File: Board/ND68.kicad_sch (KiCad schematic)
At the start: 8 parts

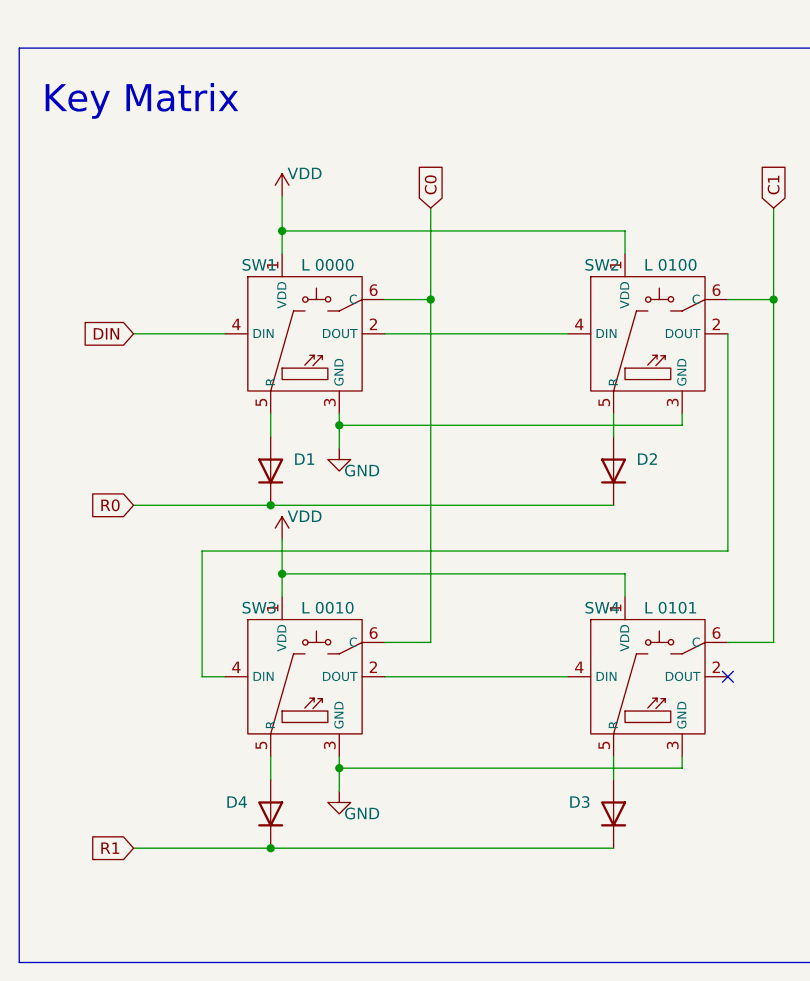
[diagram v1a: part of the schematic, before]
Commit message: Done routing all parts.
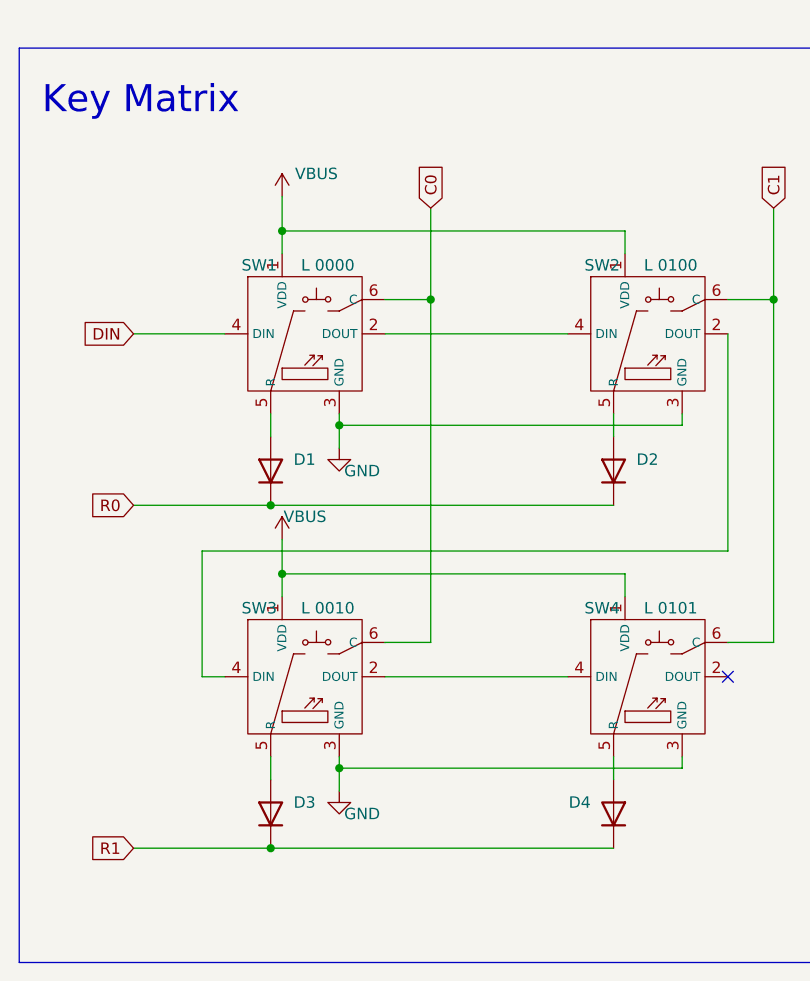
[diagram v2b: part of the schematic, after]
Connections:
- net at SW4.5 (R): now also D4.2 (A); no longer D3.2 (A)
- net at SW3.5 (R): now also D3.2 (A); no longer D4.2 (A)
- net VDD renamed VBUS
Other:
- moved on the sheet: D3, D4
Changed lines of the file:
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@@
   (junction (at 118.11 96.52) (diameter 0) (color 0 0 0 0)
   )
+  (junction (at 124.46 118.11) (diameter 0) (color 0 0 0 0)
+  )
+  (junction (at 116.84 88.9) (diameter 0) (color 0 0 0 0)
+  )
+  (junction (at 118.11 58.42) (diameter 0) (color 0 0 0 0)
+  )
+  (junction (at 124.46 80.01) (diameter 0) (color 0 0 0 0)
+  )
+  (junction (at 172.72 66.04) (diameter 0) (color 0 0 0 0)
+  )
   (junction (at 116.84 127) (diameter 0) (color 0 0 0 0)
-  )
-  (junction (at 124.46 118.11) (diameter 0) (color 0 0 0 0)
-  )
-  (junction (at 116.84 88.9) (diameter 0) (color 0 0 0 0)
-  )
-  (junction (at 118.11 58.42) (diameter 0) (color 0 0 0 0)
-  )
-  (junction (at 124.46 80.01) (diameter 0) (color 0 0 0 0)
-  )
-  (junction (at 172.72 66.04) (diameter 0) (color 0 0 0 0)
   )
   (junction (at 134.62 66.04) (diameter 0) (color 0 0 0 0)
@@
     (stroke (width 0) (type default))
   )
+  (wire (pts (xy 109.22 107.95) (xy 111.76 107.95))
+    (stroke (width 0) (type default))
+  )
+  (wire (pts (xy 101.6 69.85) (xy 111.76 69.85))
+    (stroke (width 0) (type default))
+  )
+  (wire (pts (xy 162.56 116.84) (xy 162.56 118.11))
+    (stroke (width 0) (type default))
+  )
+  (wire (pts (xy 162.56 78.74) (xy 162.56 80.01))
+    (stroke (width 0) (type default))
+  )
   (wire (pts (xy 116.84 127) (xy 154.94 127))
-    (stroke (width 0) (type default))
-  )
-  (wire (pts (xy 109.22 107.95) (xy 111.76 107.95))
-    (stroke (width 0) (type default))
-  )
-  (wire (pts (xy 101.6 69.85) (xy 111.76 69.85))
-    (stroke (width 0) (type default))
-  )
-  (wire (pts (xy 162.56 116.84) (xy 162.56 118.11))
-    (stroke (width 0) (type default))
-  )
-  (wire (pts (xy 162.56 78.74) (xy 162.56 80.01))
     (stroke (width 0) (type default))
   )
@@
     )
   )
-  (symbol (lib_id "power:VDD") (at 118.11 54.61 0) (unit 1)
+  (symbol (lib_id "power:VBUS") (at 118.11 92.71 0) (unit 1)
     (in_bom yes) (on_board yes) (dnp no)
-    (property "Reference" "#PWR028" (at 118.11 58.42 0)
-      (effects (font (size 1.27 1.27)) hide)
-    )
-    (property "Value" "VDD" (at 120.65 52.07 0)
-      (effects (font (size 1.27 1.27)))
-    )
-    (property "Footprint" "" (at 118.11 54.61 0)
-      (effects (font (size 1.27 1.27)) hide)
-    )
-    (property "Datasheet" "" (at 118.11 54.61 0)
+    (property "Reference" "#PWR028" (at 118.11 96.52 0)
+      (effects (font (size 1.27 1.27)) hide)
+    )
+    (property "Value" "VBUS" (at 120.65 90.17 0)
+      (effects (font (size 1.27 1.27)))
+    )
+    (property "Footprint" "" (at 118.11 92.71 0)
+      (effects (font (size 1.27 1.27)) hide)
+    )
+    (property "Datasheet" "" (at 118.11 92.71 0)
       (effects (font (size 1.27 1.27)) hide)
     )
@@
     )
   )
-  (symbol (lib_id "power:VDD") (at 118.11 92.71 0) (unit 1)
-    (in_bom yes) (on_board yes) (dnp no)
-    (property "Reference" "#PWR029" (at 118.11 96.52 0)
-      (effects (font (size 1.27 1.27)) hide)
-    )
-    (property "Value" "VDD" (at 120.65 90.17 0)
-      (effects (font (size 1.27 1.27)))
-    )
-    (property "Footprint" "" (at 118.11 92.71 0)
-      (effects (font (size 1.27 1.27)) hide)
-    )
-    (property "Datasheet" "" (at 118.11 92.71 0)
-      (effects (font (size 1.27 1.27)) hide)
-    )
-    (pin "1")
-    (instances
-      (project "ND68"
-        (path "/f6515d16-f8c0-46c5-adb6-b60d73ae282b"
-          (reference "#PWR029") (unit 1)
-        )
-      )
-    )
-  )
   (symbol (lib_id "Device:D") (at 154.94 85.09 90) (unit 1)
     (in_bom yes) (on_board yes) (dnp no) (fields_autoplaced)
@@
     )
   )
-  (symbol (lib_id "Device:D") (at 154.94 123.19 270) (mirror x) (unit 1)
-    (in_bom yes) (on_board yes) (dnp no) (fields_autoplaced)
-    (property "Reference" "D3" (at 152.4 121.92 90)
+  (symbol (lib_id "Device:D") (at 116.84 123.19 90) (unit 1)
+    (in_bom yes) (on_board yes) (dnp no)
+    (property "Reference" "D3" (at 119.38 121.92 90)
       (effects (font (size 1.27 1.27)) (justify right))
     )
-    (property "Value" "D" (at 152.4 124.46 90)
-      (effects (font (size 1.27 1.27)) (justify right) hide)
-    )
-    (property "Footprint" "Diode_SMD:D_SOD-123F" (at 154.94 123.19 0)
-      (effects (font (size 1.27 1.27)) hide)
-    )
-    (property "Datasheet" "https://diotec.com/request/datasheet/1n4148w.pdf" (at 154.94 123.19 0)
-      (effects (font (size 1.27 1.27)) hide)
-    )
-    (property "Sim.Device" "D" (at 154.94 123.19 0)
-      (effects (font (size 1.27 1.27)) hide)
-    )
-    (property "Sim.Pins" "1=K 2=A" (at 154.94 123.19 0)
-      (effects (font (size 1.27 1.27)) hide)
-    )
-    (property "DigiKey" "4878-1N4148WCT-ND" (at 154.94 123.19 90)
-      (effects (font (size 1.27 1.27)) hide)
-    )
-    (property "Name" "1N4148W" (at 154.94 123.19 90)
+    (property "Value" "D" (at 119.38 124.46 90)
+      (effects (font (size 1.27 1.27)) (justify right) hide)
+    )
+    (property "Footprint" "Diode_SMD:D_SOD-123F" (at 116.84 123.19 0)
+      (effects (font (size 1.27 1.27)) hide)
+    )
+    (property "Datasheet" "https://diotec.com/request/datasheet/1n4148w.pdf" (at 116.84 123.19 0)
+      (effects (font (size 1.27 1.27)) hide)
+    )
+    (property "Sim.Device" "D" (at 116.84 123.19 0)
+      (effects (font (size 1.27 1.27)) hide)
+    )
+    (property "Sim.Pins" "1=K 2=A" (at 116.84 123.19 0)
+      (effects (font (size 1.27 1.27)) hide)
+    )
+    (property "DigiKey" "4878-1N4148WCT-ND" (at 116.84 123.19 90)
+      (effects (font (size 1.27 1.27)) hide)
+    )
+    (property "Name" "1N4148W" (at 116.84 123.19 90)
       (effects (font (size 1.27 1.27)) hide)
     )
@@
         (path "/f6515d16-f8c0-46c5-adb6-b60d73ae282b"
           (reference "#PWR026") (unit 1)
+        )
+      )
+    )
+  )
+  (symbol (lib_id "power:VBUS") (at 118.11 54.61 0) (unit 1)
+    (in_bom yes) (on_board yes) (dnp no)
+    (property "Reference" "#PWR029" (at 118.11 58.42 0)
+      (effects (font (size 1.27 1.27)) hide)
+    )
+    (property "Value" "VBUS" (at 121.92 52.07 0)
+      (effects (font (size 1.27 1.27)))
+    )
+    (property "Footprint" "" (at 118.11 54.61 0)
+      (effects (font (size 1.27 1.27)) hide)
+    )
+    (property "Datasheet" "" (at 118.11 54.61 0)
+      (effects (font (size 1.27 1.27)) hide)
+    )
+    (pin "1")
+    (instances
+      (project "ND68"
+        (path "/f6515d16-f8c0-46c5-adb6-b60d73ae282b"
+          (reference "#PWR029") (unit 1)
         )
       )
@@
     )
   )
-  (symbol (lib_id "Device:D") (at 116.84 123.19 270) (mirror x) (unit 1)
-    (in_bom yes) (on_board yes) (dnp no) (fields_autoplaced)
-    (property "Reference" "D4" (at 114.3 121.92 90)
+  (symbol (lib_id "Device:D") (at 154.94 123.19 270) (mirror x) (unit 1)
+    (in_bom yes) (on_board yes) (dnp no) (fields_autoplaced)
+    (property "Reference" "D4" (at 152.4 121.92 90)
       (effects (font (size 1.27 1.27)) (justify right))
     )
-    (property "Value" "D" (at 114.3 124.46 90)
-      (effects (font (size 1.27 1.27)) (justify right) hide)
-    )
-    (property "Footprint" "Diode_SMD:D_SOD-123F" (at 116.84 123.19 0)
-      (effects (font (size 1.27 1.27)) hide)
-    )
-    (property "Datasheet" "https://diotec.com/request/datasheet/1n4148w.pdf" (at 116.84 123.19 0)
-      (effects (font (size 1.27 1.27)) hide)
-    )
-    (property "Sim.Device" "D" (at 116.84 123.19 0)
-      (effects (font (size 1.27 1.27)) hide)
-    )
-    (property "Sim.Pins" "1=K 2=A" (at 116.84 123.19 0)
-      (effects (font (size 1.27 1.27)) hide)
-    )
-    (property "DigiKey" "4878-1N4148WCT-ND" (at 116.84 123.19 90)
-      (effects (font (size 1.27 1.27)) hide)
-    )
-    (property "Name" "1N4148W" (at 116.84 123.19 90)
-      (effects (font (size 1.27 1.27)) hide)
-    )
+    (property "Value" "D" (at 152.4 124.46 90)
+      (effects (font (size 1.27 1.27)) (justify right) hide)
+    )
+    (property "Footprint" "Diode_SMD:D_SOD-123F" (at 154.94 123.19 0)
+      (effects (font (size 1.27 1.27)) hide)
+    )
+    (property "Datasheet" "https://diotec.com/request/datasheet/1n4148w.pdf" (at 154.94 123.19 0)
+      (effects (font (size 1.27 1.27)) hide)
+    )
+    (property "Sim.Device" "D" (at 154.94 123.19 0)
+      (effects (font (size 1.27 1.27)) hide)
+    )
+    (property "Sim.Pins" "1=K 2=A" (at 154.94 123.19 0)
+      (effects (font (size 1.27 1.27)) hide)
+    )
+    (property "DigiKey" "4878-1N4148WCT-ND" (at 154.94 123.19 90)
+      (effects (font (size 1.27 1.27)) hide)
+    )
+    (property "Name" "1N4148W" (at 154.94 123.19 90)
+      (effects (font (size 1.27 1.27)) hide)
+    )

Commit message: Rev 2
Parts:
- added C18, C19, C20, C21: 100n, Capacitor_SMD:C_0201_0603Metric, symbol Device:C
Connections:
- net GND: now also C18.2, C19.2, C20.2, C21.2
- net VBUS: now also C18.1, C19.1, C20.1, C21.1

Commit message: 65% ke matrix
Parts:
- removed SW2, SW3, SW4: ~, ND68:ND68-1U-HS-ARGB, symbol ND68:nd68_hotswap_argb
- added C22, C23, C24, C25, C26, C27, C28, C29, C30, C31, C32, C33, C34, C35, C36, C37, C38, C39, C40, C41, C42, C43, C44, C45, C46, C47, C48, C49, C50, C51, C52, C53, C54, C55, C56, C57, C58, C59, C60, C61, C62, C63, C64, C65, C66, C67, C68, C69, C70, C71, C72, C73, C74, C75, C76, C77, C78, C79, C80, C81, C82, C83, C84, C85: 100n, Capacitor_SMD:C_0201_0603Metric, symbol Device:C
- added D10, D11, D12, D13, D14, D15, D16, D17, D18, D19, D20, D21, D22, D23, D24, D25, D26, D27, D28, D29, D30, D31, D32, D33, D34, D35, D36, D37, D38, D39, D40, D41, D42, D43, D44, D45, D46, D47, D48, D49, D5, D50, D51, D52, D53, D54, D55, D56, D57, D58, D59, D6, D60, D61, D62, D63, D64, D65, D66, D67, D68, D7, D8, D9: D, Diode_SMD:D_SOD-123F, symbol Device:D
- added SW10, SW11, SW12, SW13, SW15, SW17, SW18, SW19, SW2, SW20, SW21, SW22, SW23, SW24, SW25, SW26, SW27, SW28, SW3, SW30, SW32, SW33, SW34, SW35, SW36, SW37, SW38, SW39, SW4, SW40, SW41, SW42, SW44, SW46, SW47, SW48, SW49, SW5, SW50, SW51, SW52, SW53, SW54, SW55, SW57, SW58, SW6, SW63, SW64, SW65, SW66, SW67, SW68, SW7, SW8, SW9: ~, ND68:ND68-1U-HS-ARGB, symbol ND68:nd68_1u_hotswap_argb
- added SW14: ~, ND68:ND68-2U-HS-ARGB, symbol ND68:nd68_2u_hotswap_argb
- added SW16, SW29: ~, ND68:ND68-1.5U-HS-ARGB, symbol ND68:nd68_1.5u_hotswap_argb
- added SW31: ~, ND68:ND68-1.5U-HS-ARGB, symbol ND68:nd68_1.75u_hotswap_argb
- added SW43, SW45: ~, ND68:ND68-2.25U-HS-ARGB, symbol ND68:nd68_2.25u_hotswap_argb
- added SW56: ~, ND68:ND68-1.75U-HS-ARGB, symbol ND68:nd68_1.75u_hotswap_argb
- added SW59, SW60, SW61: ~, ND68:ND68-1.25U-HS-ARGB, symbol ND68:nd68_1.25u_hotswap_argb
- added SW62: ~, ND68:ND68-6.25U-HS-ARGB, symbol ND68:nd68_6.25u_hotswap_argb
- SW1: symbol ND68:nd68_hotswap_argb -> ND68:nd68_1u_hotswap_argb
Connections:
- net C0: now also SW16.6 (C), SW31.6 (C), SW45.6 (C), SW59.6 (C)
- net C1: now also SW17.6 (C), SW2.6 (C), SW32.6 (C), SW46.6 (C), SW60.6 (C)
- net GND: now also SW10.3 (GND), SW11.3 (GND), SW12.3 (GND), SW13.3 (GND), SW14.3 (GND), SW15.3 (GND), SW16.3 (GND), SW17.3 (GND), SW18.3 (GND), SW19.3 (GND), SW2.3 (GND), SW20.3 (GND), SW21.3 (GND), SW22.3 (GND), SW23.3 (GND), SW24.3 (GND), SW25.3 (GND), SW26.3 (GND), SW27.3 (GND), SW28.3 (GND), SW29.3 (GND), SW3.3 (GND), SW30.3 (GND), SW31.3 (GND), SW32.3 (GND), SW33.3 (GND), SW34.3 (GND), SW35.3 (GND), SW36.3 (GND), SW37.3 (GND), SW38.3 (GND), SW39.3 (GND), SW4.3 (GND), SW40.3 (GND), SW41.3 (GND), SW42.3 (GND), SW43.3 (GND), SW44.3 (GND), SW45.3 (GND), SW46.3 (GND), SW47.3 (GND), SW48.3 (GND), SW49.3 (GND), SW5.3 (GND), SW50.3 (GND), SW51.3 (GND), SW52.3 (GND), SW53.3 (GND), SW54.3 (GND), SW55.3 (GND), SW56.3 (GND), SW57.3 (GND), SW58.3 (GND), SW59.3 (GND), SW6.3 (GND), SW60.3 (GND), SW61.3 (GND), SW62.3 (GND), SW63.3 (GND), SW64.3 (GND), SW65.3 (GND), SW66.3 (GND), SW67.3 (GND), SW68.3 (GND), SW7.3 (GND), SW8.3 (GND), SW9.3 (GND); no longer C18.2, C19.2, C20.2, C21.2
- net R0: now also D3.1 (K), D4.1 (K), D10.1 (K), D11.1 (K), D12.1 (K), D13.1 (K), D14.1 (K), D15.1 (K), D5.1 (K), D6.1 (K), D7.1 (K), D8.1 (K), D9.1 (K)
- net R1: now also D16.1 (K), D17.1 (K), D18.1 (K), D19.1 (K), D20.1 (K), D21.1 (K), D22.1 (K), D23.1 (K), D24.1 (K), D25.1 (K), D26.1 (K), D27.1 (K), D28.1 (K), D29.1 (K), D30.1 (K); no longer D3.1 (K), D4.1 (K)
- net VBUS: now also C22.1, C23.1, C24.1, C25.1, C26.1, C27.1, C28.1, C29.1, C30.1, C31.1, C32.1, C33.1, C34.1, C35.1, C36.1, C37.1, C38.1, C39.1, C40.1, C41.1, C42.1, C43.1, C44.1, C45.1, C46.1, C47.1, C48.1, C49.1, C50.1, C51.1, C52.1, C53.1, C54.1, C55.1, C56.1, C57.1, C58.1, C59.1, C60.1, C61.1, C62.1, C63.1, C64.1, C65.1, C66.1, C67.1, C68.1, C69.1, C70.1, C71.1, C72.1, C73.1, C74.1, C75.1, C76.1, C77.1, C78.1, C79.1, C80.1, C81.1, C82.1, C83.1, C84.1, C85.1; no longer SW1.1 (VDD)
- net at D4.2 (A): now also SW4.5 (R)
- net at D2.2 (A): now also SW2.5 (R)
- net at D3.2 (A): now also SW3.5 (R)
- net at SW1.2 (DOUT): now also SW2.4 (DIN)
- new net: D48.2 (A), SW48.5 (R)
- new net: D9.2 (A), SW9.5 (R)
- new net: D66.2 (A), SW66.5 (R)
- new net: C65.2, SW48.1 (VDD)
- new net: C33.2, SW16.1 (VDD)
- new net: SW16.2 (DOUT), SW17.4 (DIN)
- new net: SW15.2 (DOUT), SW16.4 (DIN)
- new net: D16.2 (A), SW16.5 (R)
- new net: C55.2, SW38.1 (VDD)
- new net: SW38.2 (DOUT), SW39.4 (DIN)
- new net: SW37.2 (DOUT), SW38.4 (DIN)
- new net: D38.2 (A), SW38.5 (R)
- new net: C72.2, SW55.1 (VDD)
- new net: D56.2 (A), SW56.5 (R)
- new net: D29.2 (A), SW29.5 (R)
- new net: C50.2, SW33.1 (VDD)
- new net: C62.2, SW45.1 (VDD)
- new net: D46.2 (A), SW46.5 (R)
- new net: C56.2, SW39.1 (VDD)
- new net: D60.2 (A), SW60.5 (R)
- new net: D43.2 (A), SW43.5 (R)
- new net: C57.2, SW40.1 (VDD)
- new net: C32.2, SW15.1 (VDD)
- new net: SW14.2 (DOUT), SW15.4 (DIN)
- new net: D15.2 (A), SW15.5 (R)
- new net: C71.2, SW54.1 (VDD)
- new net: SW54.2 (DOUT), SW55.4 (DIN)
- new net: SW53.2 (DOUT), SW54.4 (DIN)
- new net: D54.2 (A), SW54.5 (R)
- new net: C59.2, SW42.1 (VDD)
- new net: SW42.2 (DOUT), SW43.4 (DIN)
- new net: SW41.2 (DOUT), SW42.4 (DIN)
- new net: D42.2 (A), SW42.5 (R)
- new net: D39.2 (A), SW39.5 (R)
- new net: D31.2 (A), SW31.5 (R)
- new net: C38.2, SW21.1 (VDD)
- new net: C39.2, SW22.1 (VDD)
- new net: C23.2, SW6.1 (VDD)
- new net: C52.2, SW35.1 (VDD)
- new net: C63.2, SW46.1 (VDD)
- new net: SW46.2 (DOUT), SW47.4 (DIN)
- new net: SW45.2 (DOUT), SW46.4 (DIN)
- new net: C37.2, SW20.1 (VDD)
- new net: C67.2, SW50.1 (VDD)
- new net: D30.2 (A), SW30.5 (R)
- new net: D53.2 (A), SW53.5 (R)
- new net: C78.2, SW61.1 (VDD)
- new net: SW61.2 (DOUT), SW62.4 (DIN)
- new net: SW60.2 (DOUT), SW61.4 (DIN)
- new net: D61.2 (A), SW61.5 (R)
- new net: C43.2, SW26.1 (VDD)
- new net: SW26.2 (DOUT), SW27.4 (DIN)
- new net: SW25.2 (DOUT), SW26.4 (DIN)
- new net: D26.2 (A), SW26.5 (R)
- new net: D33.2 (A), SW33.5 (R)
- new net: C31.2, SW14.1 (VDD)
- new net: D64.2 (A), SW64.5 (R)
- new net: C40.2, SW23.1 (VDD)
- new net: SW23.2 (DOUT), SW24.4 (DIN)
- new net: SW22.2 (DOUT), SW23.4 (DIN)
- new net: D23.2 (A), SW23.5 (R)
- new net: C36.2, SW19.1 (VDD)
- new net: D58.2 (A), SW58.5 (R)
- new net: C44.2, SW27.1 (VDD)
- new net: SW27.2 (DOUT), SW28.4 (DIN)
- new net: D27.2 (A), SW27.5 (R)
- new net: C79.2, SW62.1 (VDD)
- new net: SW62.2 (DOUT), SW63.4 (DIN)
- new net: D62.2 (A), SW62.5 (R)
- new net: D14.2 (A), SW14.5 (R)
- new net: C20.2, SW3.1 (VDD)
- new net: SW3.2 (DOUT), SW4.4 (DIN)
- new net: SW2.2 (DOUT), SW3.4 (DIN)
- new net: C83.2, SW66.1 (VDD)
- new net: D37.2 (A), SW37.5 (R)
- new net: C48.2, SW31.1 (VDD)
- new net: SW31.2 (DOUT), SW32.4 (DIN)
- new net: SW30.2 (DOUT), SW31.4 (DIN)
- new net: D19.2 (A), SW19.5 (R)
- new net: C61.2, SW44.1 (VDD)
- new net: SW44.2 (DOUT), SW45.4 (DIN)
- new net: SW43.2 (DOUT), SW44.4 (DIN)
- new net: D44.2 (A), SW44.5 (R)
- new net: C47.2, SW30.1 (VDD)
- new net: C70.2, SW53.1 (VDD)
- new net: SW52.2 (DOUT), SW53.4 (DIN)
- new net: C53.2, SW36.1 (VDD)
- new net: C81.2, SW64.1 (VDD)
- new net: SW64.2 (DOUT), SW65.4 (DIN)
- new net: SW63.2 (DOUT), SW64.4 (DIN)
- new net: C68.2, SW51.1 (VDD)
- new net: D65.2 (A), SW65.5 (R)
- new net: C58.2, SW41.1 (VDD)
- new net: SW40.2 (DOUT), SW41.4 (DIN)
- new net: D41.2 (A), SW41.5 (R)
- new net: SW33.2 (DOUT), SW34.4 (DIN)
- new net: SW32.2 (DOUT), SW33.4 (DIN)
- new net: C60.2, SW43.1 (VDD)
- new net: C25.2, SW8.1 (VDD)
- new net: C49.2, SW32.1 (VDD)
- new net: SW50.2 (DOUT), SW51.4 (DIN)
- new net: SW49.2 (DOUT), SW50.4 (DIN)
- new net: D50.2 (A), SW50.5 (R)
- new net: C69.2, SW52.1 (VDD)
- new net: SW51.2 (DOUT), SW52.4 (DIN)
- new net: D52.2 (A), SW52.5 (R)
- new net: C76.2, SW59.1 (VDD)
- new net: SW59.2 (DOUT), SW60.4 (DIN)
- new net: SW58.2 (DOUT), SW59.4 (DIN)
- new net: D59.2 (A), SW59.5 (R)
- new net: SW13.2 (DOUT), SW14.4 (DIN)
- new net: C66.2, SW49.1 (VDD)
- new net: SW48.2 (DOUT), SW49.4 (DIN)
- new net: D49.2 (A), SW49.5 (R)
- new net: D47.2 (A), SW47.5 (R)
- new net: D36.2 (A), SW36.5 (R)
- new net: C77.2, SW60.1 (VDD)
- new net: D6.2 (A), SW6.5 (R)
- new net: D55.2 (A), SW55.5 (R)
- new net: SW39.2 (DOUT), SW40.4 (DIN)
- new net: C34.2, SW17.1 (VDD)
- new net: SW17.2 (DOUT), SW18.4 (DIN)
- new net: D17.2 (A), SW17.5 (R)
- new net: D34.2 (A), SW34.5 (R)
- new net: D40.2 (A), SW40.5 (R)
- new net: C27.2, SW10.1 (VDD)
- new net: SW10.2 (DOUT), SW11.4 (DIN)
- new net: SW10.4 (DIN), SW9.2 (DOUT)
- new net: D10.2 (A), SW10.5 (R)
- new net: D51.2 (A), SW51.5 (R)
- new net: SW21.2 (DOUT), SW22.4 (DIN)
- new net: SW20.2 (DOUT), SW21.4 (DIN)
- new net: D21.2 (A), SW21.5 (R)
- new net: D24.2 (A), SW24.5 (R)
- new net: C42.2, SW25.1 (VDD)
- new net: SW24.2 (DOUT), SW25.4 (DIN)
- new net: D25.2 (A), SW25.5 (R)
- new net: SW6.2 (DOUT), SW7.4 (DIN)
- new net: SW5.2 (DOUT), SW6.4 (DIN)
- new net: C54.2, SW37.1 (VDD)
- new net: SW36.2 (DOUT), SW37.4 (DIN)
- new net: C74.2, SW57.1 (VDD)
- new net: SW57.2 (DOUT), SW58.4 (DIN)
- new net: SW56.2 (DOUT), SW57.4 (DIN)
- new net: D57.2 (A), SW57.5 (R)
- new net: D28.2 (A), SW28.5 (R)
- new net: C64.2, SW47.1 (VDD)
- new net: D63.2 (A), SW63.5 (R)
- new net: C21.2, SW4.1 (VDD)
- new net: SW4.2 (DOUT), SW5.4 (DIN)
- new net: SW29.2 (DOUT), SW30.4 (DIN)
- new net: C22.2, SW5.1 (VDD)
- new net: D68.2 (A), SW68.5 (R)
- new net: C45.2, SW28.1 (VDD)
- new net: SW28.2 (DOUT), SW29.4 (DIN)
- new net: C28.2, SW11.1 (VDD)
- new net: SW11.2 (DOUT), SW12.4 (DIN)
- new net: D11.2 (A), SW11.5 (R)
- new net: D5.2 (A), SW5.5 (R)
- new net: C24.2, SW7.1 (VDD)
- new net: SW7.2 (DOUT), SW8.4 (DIN)
- new net: D7.2 (A), SW7.5 (R)
- new net: C41.2, SW24.1 (VDD)
- new net: D12.2 (A), SW12.5 (R)
- new net: C19.2, SW2.1 (VDD)
- new net: C29.2, SW12.1 (VDD)
- new net: SW12.2 (DOUT), SW13.4 (DIN)
- new net: C80.2, SW63.1 (VDD)
- new net: C51.2, SW34.1 (VDD)
- new net: SW34.2 (DOUT), SW35.4 (DIN)
- new net: D32.2 (A), SW32.5 (R)
- new net: D67.2 (A), SW67.5 (R)
- new net: C85.2, SW68.1 (VDD)
- new net: SW67.2 (DOUT), SW68.4 (DIN)
- new net: D8.2 (A), SW8.5 (R)
- new net: C75.2, SW58.1 (VDD)
- new net: C18.2, SW1.1 (VDD)
- new net: D13.2 (A), SW13.5 (R)
- new net: D22.2 (A), SW22.5 (R)
- new net: C84.2, SW67.1 (VDD)
- new net: C30.2, SW13.1 (VDD)
- new net: C46.2, SW29.1 (VDD)
- new net: C73.2, SW56.1 (VDD)
- new net: SW19.2 (DOUT), SW20.4 (DIN)
- new net: SW18.2 (DOUT), SW19.4 (DIN)
- new net: SW47.2 (DOUT), SW48.4 (DIN)
- new net: SW55.2 (DOUT), SW56.4 (DIN)
- new net: SW66.2 (DOUT), SW67.4 (DIN)
- new net: SW65.2 (DOUT), SW66.4 (DIN)
- new net: SW35.2 (DOUT), SW36.4 (DIN)
- new net: C82.2, SW65.1 (VDD)
- new net: C26.2, SW9.1 (VDD)
- new net: SW8.2 (DOUT), SW9.4 (DIN)
- new net: D20.2 (A), SW20.5 (R)
- new net: C35.2, SW18.1 (VDD)
- new net: D18.2 (A), SW18.5 (R)
- new net: D45.2 (A), SW45.5 (R)
- new net: D35.2 (A), SW35.5 (R)
- new net C10: SW11.6 (C), SW26.6 (C), SW41.6 (C), SW55.6 (C)
- new net C11: SW12.6 (C), SW27.6 (C), SW42.6 (C), SW56.6 (C)
- new net C12: SW13.6 (C), SW28.6 (C), SW43.6 (C), SW57.6 (C)
- new net C13: SW14.6 (C), SW29.6 (C), SW44.6 (C), SW58.6 (C)
- new net C14: SW15.6 (C), SW30.6 (C)
- new net C2: SW18.6 (C), SW3.6 (C), SW33.6 (C), SW47.6 (C), SW61.6 (C)
- new net C3: SW19.6 (C), SW34.6 (C), SW4.6 (C), SW48.6 (C), SW62.6 (C)
- new net C4: SW20.6 (C), SW35.6 (C), SW49.6 (C), SW5.6 (C), SW63.6 (C)
- new net C5: SW21.6 (C), SW36.6 (C), SW50.6 (C), SW6.6 (C), SW64.6 (C)
- new net C6: SW22.6 (C), SW37.6 (C), SW51.6 (C), SW65.6 (C), SW7.6 (C)
- new net C7: SW23.6 (C), SW38.6 (C), SW52.6 (C), SW66.6 (C), SW8.6 (C)
- new net C8: SW24.6 (C), SW39.6 (C), SW53.6 (C), SW67.6 (C), SW9.6 (C)
- new net C9: SW10.6 (C), SW25.6 (C), SW40.6 (C), SW54.6 (C), SW68.6 (C)
- new net R2: D31.1 (K), D32.1 (K), D33.1 (K), D34.1 (K), D35.1 (K), D36.1 (K), D37.1 (K), D38.1 (K), D39.1 (K), D40.1 (K), D41.1 (K), D42.1 (K), D43.1 (K), D44.1 (K)
- new net R3: D45.1 (K), D46.1 (K), D47.1 (K), D48.1 (K), D49.1 (K), D50.1 (K), D51.1 (K), D52.1 (K), D53.1 (K), D54.1 (K), D55.1 (K), D56.1 (K), D57.1 (K), D58.1 (K)
- new net R4: D59.1 (K), D60.1 (K), D61.1 (K), D62.1 (K), D63.1 (K), D64.1 (K), D65.1 (K), D66.1 (K), D67.1 (K), D68.1 (K)
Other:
- moved on the sheet: C18, D1

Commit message: Added 2 leds
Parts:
- added C86, C87: 100n, Capacitor_SMD:C_0201_0603Metric, symbol Device:C
- added U4, U5: ~, ND68:ND68-1U-ARGB_LED_ONLY, symbol ND68:nd68_argb
- SW59: RC L CNRN -> L 0004
- SW60: RC L CNRN -> L 0104
- SW61: RC L CNRN -> L 0204
- SW62: RC L CNRN -> L 0304
- SW63: RC L 0403 -> L 0404
- SW64: RC L 0503 -> L 0504
- SW65: RC L 0603 -> L 0604
- SW66: RC L 0703 -> L 0704
- SW67: RC L 0803 -> L 0804
- SW68: RC L 0903 -> L 0904
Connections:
- net GND: now also U4.3 (GND), U5.3 (GND)
- net VBUS: now also C86.1, C87.1
- net at SW61.2 (DOUT): now also U4.4 (DIN); no longer SW62.4 (DIN)
- net at SW62.2 (DOUT): now also U5.4 (DIN); no longer SW63.4 (DIN)
- new net: SW62.4 (DIN), U4.2 (DOUT)
- new net: C86.2, U5.1 (VDD)
- new net: SW63.4 (DIN), U5.2 (DOUT)
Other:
- moved on the sheet: C18, C19, C20, C21, C22, C23, C24, C25, C26, C27, C28, C29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

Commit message: Change led decoupler type
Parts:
- added C88, C89: 10u, Capacitor_SMD:C_0805_2012Metric, symbol Device:C
- C18, C19, C20, C21, C22, C23, C24, C25, C26, C27, C28, C29, C30, C31, C32, C33, C34, C35, C36, C37, C38, C39, C40, C41, C42, C43, C44, C45, C46, C47, C48, C49, C50, C51, C52, C53, C54, C55, C56, C57, C58, C59, C60, C61, C62, C63, C64, C65, C66, C67, C68, C69, C70, C71, C72, C73, C74, C75, C76, C77, C78, C79, C80, C81, C82, C83, C84, C85, C86, C87: footprint Capacitor_SMD:C_0201_0603Metric -> Capacitor_SMD:C_0603_1608Metric; DigiKey 1276-1013-1-ND -> 311-1088-2-ND
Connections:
- net GND: now also C88.2, C89.2
- net VBUS: now also C88.1, C89.1
- net at U5.1 (VDD): now also C87.2; no longer C86.2
- net at U4.1 (VDD): now also C86.2
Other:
- moved on the sheet: C86, C87
